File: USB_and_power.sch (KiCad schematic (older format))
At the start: 44 parts, among them J1 USB_B_Micro, U1 LM2594M-3.3, U2 93LC54B, U3 FT4232H, Y1 12MHz

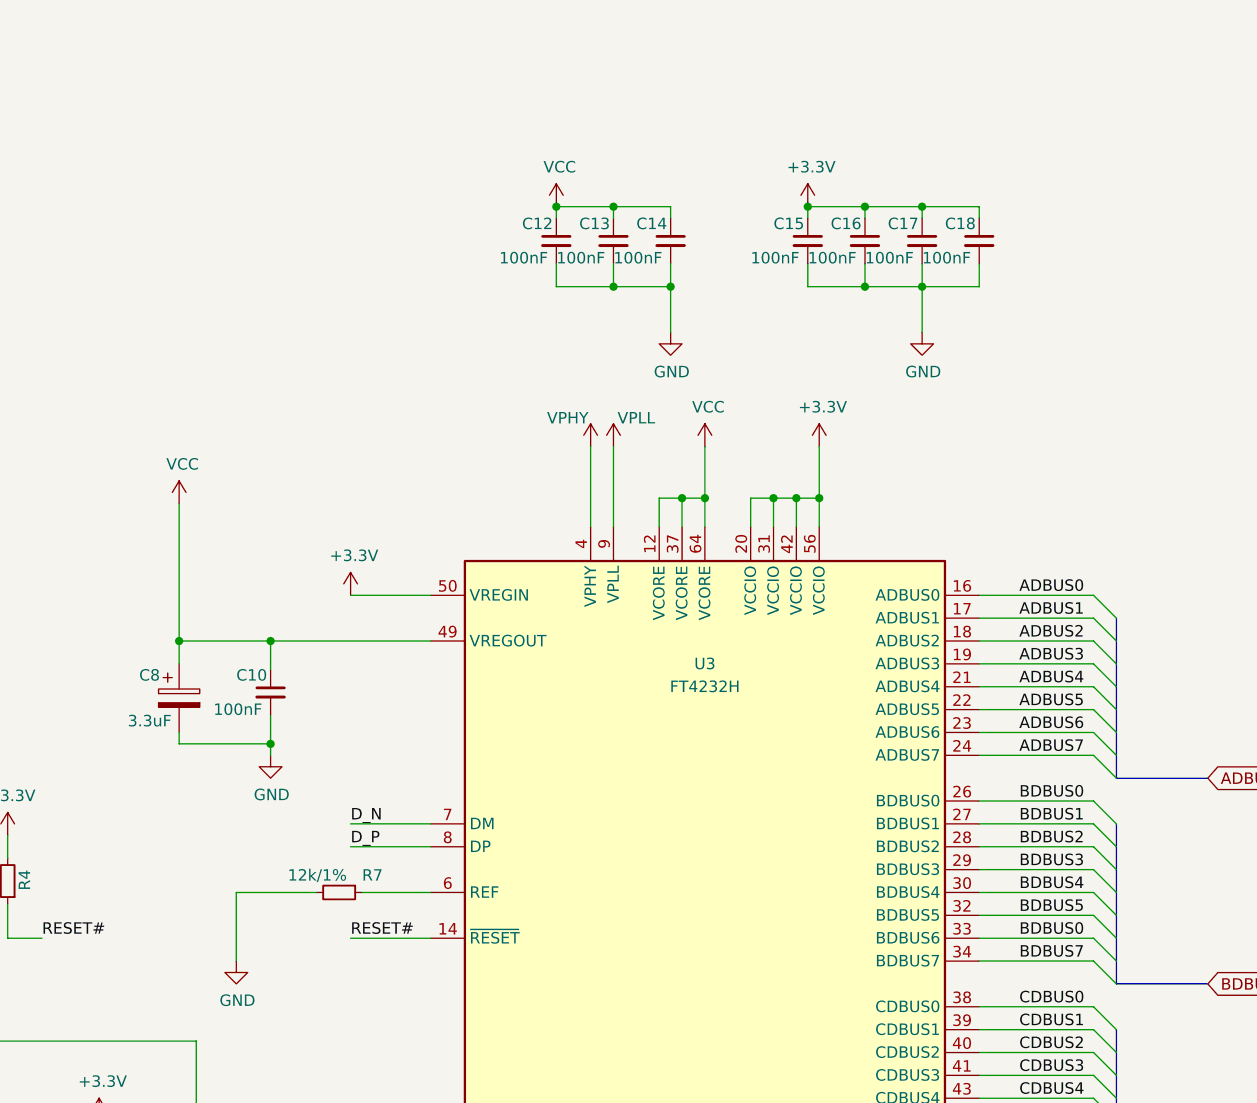
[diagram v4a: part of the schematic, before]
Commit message: Almost fully routed.. lots of DRC's to sort out.
Also need to get correct pcb parameters to do more checks.
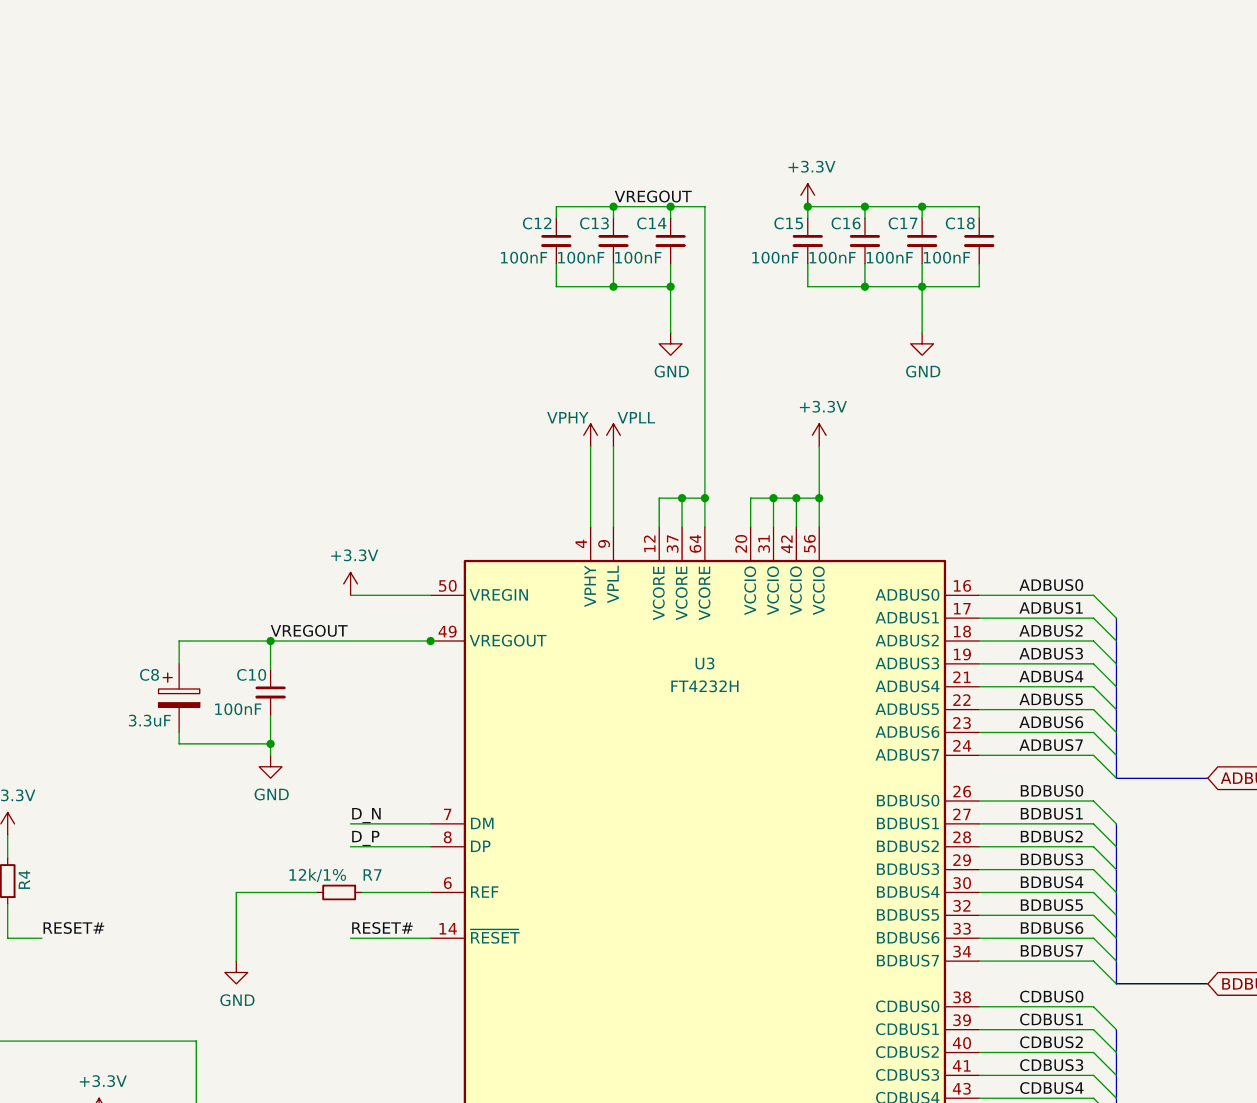
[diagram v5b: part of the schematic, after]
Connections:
- net BDBUS0: no longer U3.33 (BDBUS6)
- net VCC renamed VREGOUT
- new net BDBUS6: U3.33 (BDBUS6)
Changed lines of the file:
@@
 Text Label 9500 6250 0    50   ~ 0
 D_P
-Wire Wire Line
-	8750 5350 8750 4750
 $Comp
 L Device:CP C8
@@
 Wire Wire Line
 	9150 5475 9150 5350
-Connection ~ 8750 5350
-Connection ~ 9150 5350
-Wire Wire Line
-	9150 5350 8750 5350
 Wire Wire Line
 	8750 5800 9150 5800
@@
 Wire Wire Line
 	10950 4725 10950 4850
-Connection ~ 11050 4725
-Wire Wire Line
-	11050 4725 11050 4500
 Wire Wire Line
 	10950 4725 10850 4725
@@
 Wire Wire Line
 	10550 4850 10550 4500
-$Comp
-L power:VCC #PWR0109
-U 1 1 61296F5B
-P 11050 4500
-F 0 "#PWR0109" H 11050 4350 50  0001 C CNN
-F 1 "VCC" H 11065 4673 50  0000 C CNN
-F 2 "" H 11050 4500 50  0001 C CNN
-F 3 "" H 11050 4500 50  0001 C CNN
-	1    11050 4500
-	1    0    0    -1
-$EndComp
-$Comp
-L power:VCC #PWR0110
-U 1 1 61297529
-P 8750 4750
-F 0 "#PWR0110" H 8750 4600 50  0001 C CNN
-F 1 "VCC" H 8765 4923 50  0000 C CNN
-F 2 "" H 8750 4750 50  0001 C CNN
-F 3 "" H 8750 4750 50  0001 C CNN
-	1    8750 4750
-	1    0    0    -1
-$EndComp
 Wire Wire Line
 	9850 5150 9500 5150
@@
 	1    0    0    -1
 $EndComp
-Wire Wire Line
-	9150 5350 9850 5350
 Wire Wire Line
 	9850 6450 9550 6450
@@
 Wire Wire Line
 	10900 4000 10900 3800
-$Comp
-L power:VCC #PWR0119
-U 1 1 612E2765
-P 10400 3450
-F 0 "#PWR0119" H 10400 3300 50  0001 C CNN
-F 1 "VCC" H 10415 3623 50  0000 C CNN
-F 2 "" H 10400 3450 50  0001 C CNN
-F 3 "" H 10400 3450 50  0001 C CNN
-	1    10400 3450
-	1    0    0    -1
-$EndComp
-Connection ~ 10400 3450
 $Comp
 L local:VPHY #PWR0120
@@
 BDBUS5
 Text Label 12425 6650 0    50   ~ 0
-BDBUS0
+BDBUS6
 Text Label 12425 6750 0    50   ~ 0
 BDBUS7
@@
 Text Label 1720 4900 0    50   ~ 0
 D-
+Wire Wire Line
+	8750 5350 9150 5350
+Connection ~ 9150 5350
+Wire Wire Line
+	9150 5350 9850 5350
+Connection ~ 9850 5350
+Wire Wire Line
+	9850 5350 9855 5350
+Text Label 9150 5350 0    50   ~ 0
+VREGOUT
+Wire Wire Line
+	11050 4725 11050 3450
+Wire Wire Line
+	11050 3450 10900 3450
 Wire Bus Line
 	12850 5250 12850 5950
@@
 Wire Bus Line
 	12850 7950 12850 8650
+Connection ~ 11050 4725
+Connection ~ 10900 3450
+Text Label 10655 3450 0    50   ~ 0
+VREGOUT
 $EndSCHEMATC
